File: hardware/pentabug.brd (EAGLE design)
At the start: 82.9 x 33 mm, 19 parts, among them IC1 ATMEGA88

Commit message: bad bug fixed: removed cutout for vibra motor
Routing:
- net GND: track 57.0 -> 25.3 mm
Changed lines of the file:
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@@
 <text x="10.16" y="22.86" size="1.016" layer="25" font="vector" ratio="10">https://github.com/c3d2/pentabug</text>
 <text x="36.195" y="1.27" size="1.016" layer="30" font="vector" ratio="10" rot="MR0">https://github.com/c3d2/pentabug</text>
-<text x="37.465" y="22.86" size="1.4224" layer="30" font="vector" ratio="14" rot="MR0">Pentabug V1.0</text>
+<text x="36.83" y="22.86" size="1.4224" layer="30" font="vector" ratio="14" rot="MR0">Pentabug V1.0</text>
 </plain>
 <attributes>
@@
 <via x="3.81" y="22.86" extent="1-16" drill="0.6" alwaysstop="yes"/>
 <via x="4.445" y="21.59" extent="1-16" drill="0.6" alwaysstop="yes"/>
-<wire x1="4.445" y1="21.59" x2="4.445" y2="11.43" width="1.27" layer="16"/>
 <wire x1="41.91" y1="12.7" x2="41.91" y2="11.43" width="0.6096" layer="1"/>
 <wire x1="41.91" y1="11.43" x2="42.545" y2="10.795" width="0.6096" layer="1"/>
@@
 <wire x1="55.1688" y1="2.1844" x2="52.07" y2="6.35" width="0.6096" layer="1"/>
 <wire x1="52.07" y1="6.35" x2="46.99" y2="7.62" width="0.6096" layer="1"/>
-<wire x1="4.445" y1="21.59" x2="4.445" y2="10.16" width="1.4224" layer="1"/>
 <wire x1="4.445" y1="10.16" x2="3.81" y2="10.16" width="1.4224" layer="1"/>
 <via x="17.145" y="7.62" extent="1-16" drill="0.6"/>
@@
 <via x="48.26" y="3.175" extent="1-16" drill="0.6"/>
 <via x="76.835" y="31.115" extent="1-16" drill="0.6"/>
-<wire x1="8.5" y1="21.59" x2="8.5" y2="11.43" width="1.9304" layer="16"/>
 <via x="5.715" y="8.89" extent="1-16" drill="1.4"/>
 <via x="5.715" y="24.13" extent="1-16" drill="1.4"/>

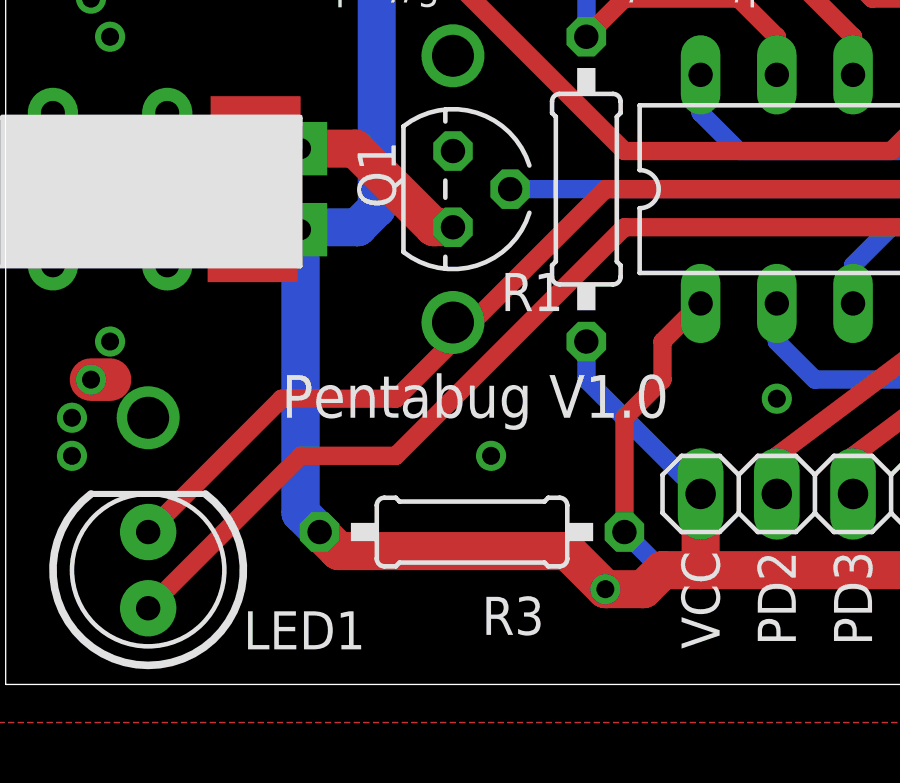
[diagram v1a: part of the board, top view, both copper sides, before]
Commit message: fixed bad bad evil vias connecting Vcc and GND
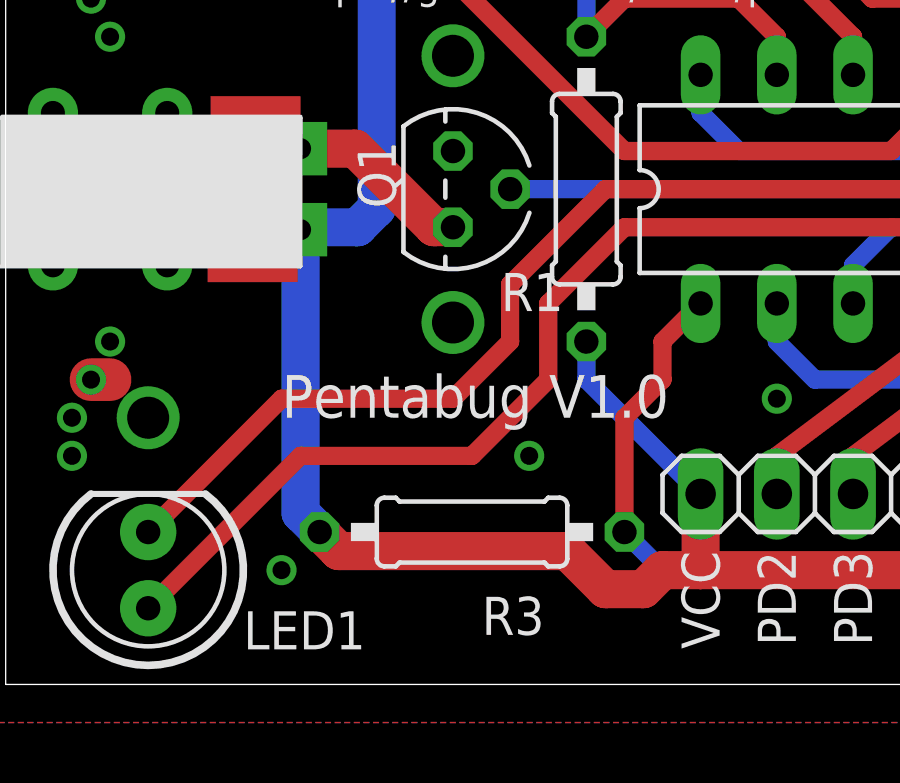
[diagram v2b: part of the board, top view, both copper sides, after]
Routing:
- net N$3: track 39.2 -> 40.7 mm
- net N$10: track 35.6 -> 36.7 mm
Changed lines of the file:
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@@
 <via x="73.66" y="17.78" extent="1-16" drill="0.6"/>
 <via x="73.66" y="20.32" extent="1-16" drill="0.6"/>
-<via x="20.955" y="3.175" extent="1-16" drill="0.6"/>
+<via x="10.16" y="3.81" extent="1-16" drill="0.6"/>
 <via x="3.175" y="7.62" extent="1-16" drill="0.6" alwaysstop="yes"/>
 <via x="3.175" y="8.89" extent="1-16" drill="0.6" alwaysstop="yes"/>
@@
 <wire x1="52.07" y1="6.35" x2="46.99" y2="7.62" width="0.6096" layer="1"/>
 <wire x1="4.445" y1="10.16" x2="3.81" y2="10.16" width="1.4224" layer="1"/>
-<via x="17.145" y="7.62" extent="1-16" drill="0.6"/>
+<via x="18.415" y="7.62" extent="1-16" drill="0.6"/>
 <via x="26.67" y="9.525" extent="1-16" drill="0.6"/>
 <via x="18.415" y="24.765" extent="1-16" drill="0.6"/>
@@
 <wire x1="33.02" y1="15.24" x2="36.83" y2="19.05" width="0.6096" layer="1"/>
 <wire x1="36.83" y1="19.05" x2="36.83" y2="20.32" width="0.6096" layer="1"/>
-<wire x1="21.59" y1="15.24" x2="13.97" y2="7.62" width="0.6096" layer="1"/>
-<wire x1="13.97" y1="7.62" x2="10.795" y2="7.62" width="0.6096" layer="1"/>
+<wire x1="16.51" y1="7.62" x2="10.795" y2="7.62" width="0.6096" layer="1"/>
+<wire x1="21.59" y1="15.24" x2="19.05" y2="12.7" width="0.6096" layer="1"/>
+<wire x1="19.05" y1="12.7" x2="19.05" y2="10.16" width="0.6096" layer="1"/>
+<wire x1="19.05" y1="10.16" x2="16.51" y2="7.62" width="0.6096" layer="1"/>
 </signal>
 <signal name="N$5">
@@
 <wire x1="31.75" y1="16.51" x2="34.29" y2="19.05" width="0.6096" layer="1"/>
 <wire x1="34.29" y1="19.05" x2="34.29" y2="20.32" width="0.6096" layer="1"/>
-<wire x1="20.955" y1="16.51" x2="13.97" y2="9.525" width="0.6096" layer="1"/>
-<wire x1="13.97" y1="9.525" x2="10.16" y2="9.525" width="0.6096" layer="1"/>
+<wire x1="15.875" y1="9.525" x2="10.16" y2="9.525" width="0.6096" layer="1"/>
+<wire x1="20.955" y1="16.51" x2="17.78" y2="13.335" width="0.6096" layer="1"/>
+<wire x1="17.78" y1="13.335" x2="17.78" y2="11.43" width="0.6096" layer="1"/>
+<wire x1="17.78" y1="11.43" x2="15.875" y2="9.525" width="0.6096" layer="1"/>
 </signal>
 <signal name="BATTLVL">

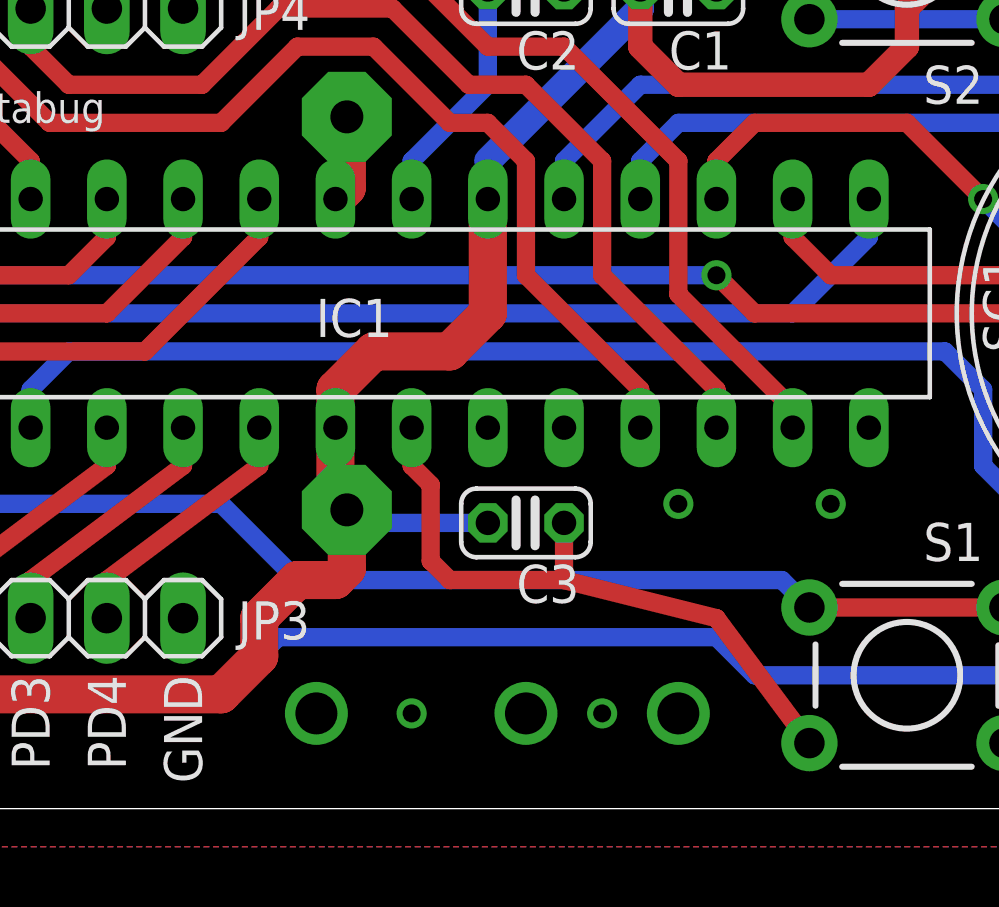
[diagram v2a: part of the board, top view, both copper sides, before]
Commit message: c3 closer to uC, "resistor" between avcc and vcc
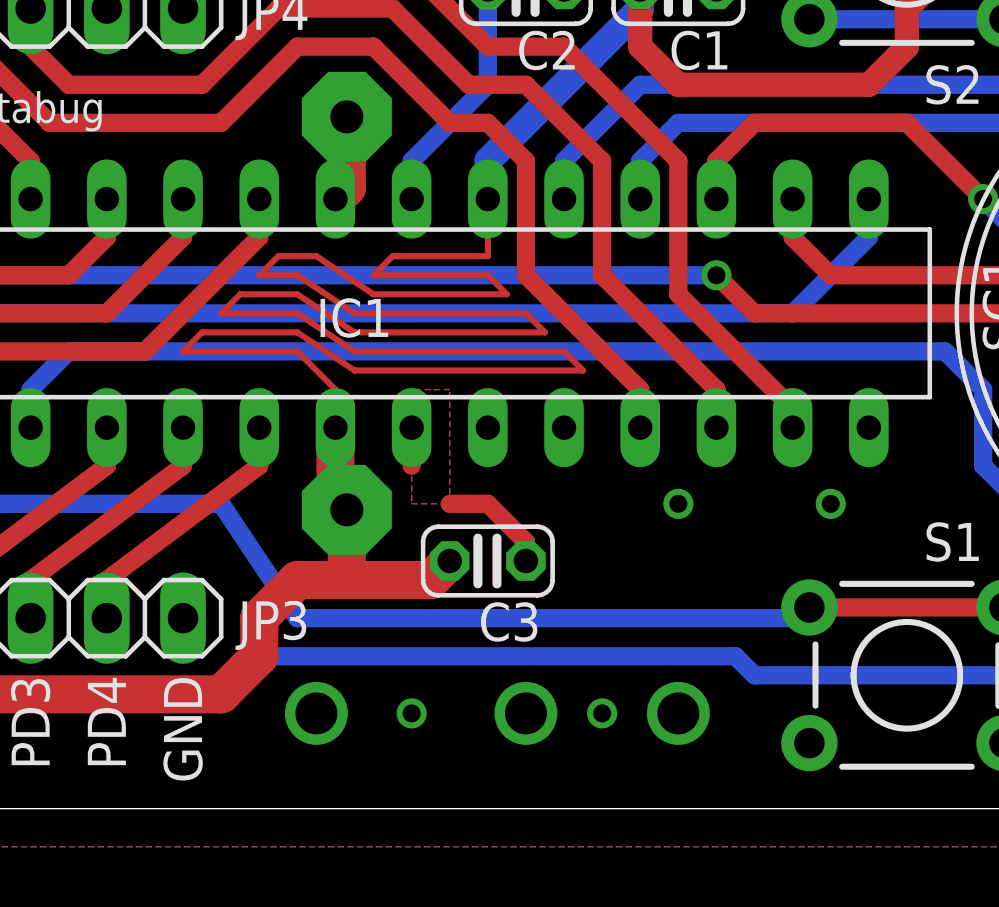
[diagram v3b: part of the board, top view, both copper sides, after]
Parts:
- moved C3 1.80 mm to (44.5, 8.26)
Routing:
- net VCC: track 142.5 -> 205.3 mm
- net GND: track 25.3 -> 8.50 mm, vias 42 -> 44
- net RX: track 51.0 -> 51.8 mm
- net RST: track 81.2 -> 80.7 mm
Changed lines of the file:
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@@
 <layer number="21" name="tPlace" color="7" fill="1" visible="yes" active="yes"/>
 <layer number="22" name="bPlace" color="7" fill="1" visible="yes" active="yes"/>
-<layer number="23" name="tOrigins" color="15" fill="1" visible="no" active="yes"/>
-<layer number="24" name="bOrigins" color="15" fill="1" visible="no" active="yes"/>
-<layer number="25" name="tNames" color="7" fill="1" visible="yes" active="yes"/>
-<layer number="26" name="bNames" color="7" fill="1" visible="no" active="yes"/>
+<layer number="23" name="tOrigins" color="15" fill="1" visible="yes" active="yes"/>
+<layer number="24" name="bOrigins" color="15" fill="1" visible="yes" active="yes"/>
+<layer number="25" name="tNames" color="7" fill="1" visible="no" active="yes"/>
+<layer number="26" name="bNames" color="7" fill="1" visible="yes" active="yes"/>
 <layer number="27" name="tValues" color="7" fill="1" visible="no" active="yes"/>
 <layer number="28" name="bValues" color="7" fill="1" visible="no" active="yes"/>
@@
 <param name="mdDrill" value="8mil"/>
 <param name="mdSmdStop" value="0mil"/>
-<param name="msWidth" value="10mil"/>
+<param name="msWidth" value="8mil"/>
 <param name="msDrill" value="0.6mm"/>
 <param name="msMicroVia" value="9.99mm"/>
@@
 <attribute name="NAME" x="60.96" y="9.525" size="1.27" layer="25" font="vector" ratio="10" rot="R180"/>
 </element>
-<element name="C3" library="resistor" package="C025-024X044" value="100nF" x="45.72" y="9.525" smashed="yes" rot="R180">
-<attribute name="NAME" x="47.498" y="8.128" size="1.27" layer="25" font="vector" ratio="10" rot="R180"/>
-<attribute name="VALUE" x="47.498" y="12.192" size="1.27" layer="27" ratio="10" rot="R180"/>
+<element name="C3" library="resistor" package="C025-024X044" value="100nF" x="44.45" y="8.255" smashed="yes" rot="R180">
+<attribute name="NAME" x="46.228" y="6.858" size="1.27" layer="25" font="vector" ratio="10" rot="R180"/>
+<attribute name="VALUE" x="46.228" y="10.922" size="1.27" layer="27" ratio="10" rot="R180"/>
 </element>
 <element name="Q1" library="transistors" package="TO-92" value="" x="15.875" y="16.51" smashed="yes" rot="R270">
@@
 </element>
 <element name="BAT1" library="seb" package="BATTERY_2XAAA" value="BATTERY_2XAAA" x="63.5" y="16.51" smashed="yes" rot="MR180">
-<attribute name="NAME" x="36.83" y="3.048" size="1.27" layer="26" font="vector" ratio="10" rot="MR180"/>
+<attribute name="NAME" x="60.325" y="2.667" size="1.27" layer="26" font="vector" ratio="10" rot="MR0"/>
 <attribute name="VALUE" x="36.83" y="32.385" size="1.778" layer="28" font="vector" ratio="10" rot="MR180"/>
 </element>
@@
 <contactref element="BAT1" pad="+"/>
 <contactref element="U$1" pad="P$1"/>
-<wire x1="39.37" y1="12.7" x2="39.37" y2="13.97" width="1.27" layer="1"/>
-<wire x1="39.37" y1="13.97" x2="40.64" y2="15.24" width="1.27" layer="1"/>
-<wire x1="40.64" y1="15.24" x2="43.18" y2="15.24" width="1.27" layer="1"/>
-<wire x1="43.18" y1="15.24" x2="44.45" y2="16.51" width="1.27" layer="1"/>
-<wire x1="44.45" y1="16.51" x2="44.45" y2="20.32" width="1.27" layer="1"/>
 <wire x1="44.45" y1="20.32" x2="44.45" y2="21.59" width="0.6096" layer="16"/>
 <wire x1="44.45" y1="21.59" x2="49.53" y2="26.67" width="0.9144" layer="16"/>
@@
 <wire x1="62.865" y1="28.575" x2="63.805" y2="27.635" width="0.8128" layer="1"/>
 <wire x1="67.945" y1="27.635" x2="70.79" y2="30.48" width="0.8128" layer="1"/>
-<wire x1="44.45" y1="9.525" x2="40.185" y2="9.525" width="0.6096" layer="16"/>
-<wire x1="40.185" y1="9.525" x2="39.75" y2="9.96" width="0.6096" layer="16"/>
+<wire x1="43.18" y1="8.255" x2="42.545" y2="7.62" width="1.27" layer="1"/>
+<wire x1="42.545" y1="7.62" x2="39.37" y2="7.62" width="1.27" layer="1"/>
+<wire x1="39.37" y1="12.7" x2="39.37" y2="13.97" width="0.2032" layer="1"/>
+<wire x1="39.37" y1="13.97" x2="38.1" y2="15.24" width="0.2032" layer="1"/>
+<wire x1="38.1" y1="15.24" x2="34.29" y2="15.24" width="0.2032" layer="1"/>
+<wire x1="34.29" y1="15.24" x2="34.925" y2="15.875" width="0.2032" layer="1"/>
+<wire x1="34.925" y1="15.875" x2="38.1" y2="15.875" width="0.2032" layer="1"/>
+<wire x1="38.1" y1="15.875" x2="40.005" y2="14.605" width="0.2032" layer="1"/>
+<wire x1="40.005" y1="14.605" x2="47.625" y2="14.605" width="0.2032" layer="1"/>
+<wire x1="47.625" y1="14.605" x2="46.99" y2="15.24" width="0.2032" layer="1"/>
+<wire x1="46.99" y1="15.24" x2="40.005" y2="15.24" width="0.2032" layer="1"/>
+<wire x1="40.005" y1="15.24" x2="38.1" y2="16.51" width="0.2032" layer="1"/>
+<wire x1="38.1" y1="16.51" x2="35.56" y2="16.51" width="0.2032" layer="1"/>
+<wire x1="35.56" y1="16.51" x2="36.195" y2="17.145" width="0.2032" layer="1"/>
+<wire x1="36.195" y1="17.145" x2="38.1" y2="17.145" width="0.2032" layer="1"/>
+<wire x1="38.1" y1="17.145" x2="40.005" y2="15.875" width="0.2032" layer="1"/>
+<wire x1="40.005" y1="15.875" x2="46.355" y2="15.875" width="0.2032" layer="1"/>
+<wire x1="46.355" y1="15.875" x2="45.72" y2="16.51" width="0.2032" layer="1"/>
+<wire x1="45.72" y1="16.51" x2="40.005" y2="16.51" width="0.2032" layer="1"/>
+<wire x1="40.005" y1="16.51" x2="38.1" y2="17.78" width="0.2032" layer="1"/>
+<wire x1="38.1" y1="17.78" x2="36.83" y2="17.78" width="0.2032" layer="1"/>
+<wire x1="36.83" y1="17.78" x2="37.465" y2="18.415" width="0.2032" layer="1"/>
+<wire x1="37.465" y1="18.415" x2="38.735" y2="18.415" width="0.2032" layer="1"/>
+<wire x1="38.735" y1="18.415" x2="40.64" y2="17.145" width="0.2032" layer="1"/>
+<wire x1="40.64" y1="17.145" x2="45.085" y2="17.145" width="0.2032" layer="1"/>
+<wire x1="45.085" y1="17.145" x2="44.45" y2="17.78" width="0.2032" layer="1"/>
+<wire x1="44.45" y1="17.78" x2="40.64" y2="17.78" width="0.2032" layer="1"/>
+<wire x1="40.64" y1="17.78" x2="41.275" y2="18.415" width="0.2032" layer="1"/>
+<wire x1="41.275" y1="18.415" x2="44.45" y2="18.415" width="0.2032" layer="1"/>
+<wire x1="44.45" y1="18.415" x2="44.45" y2="20.32" width="0.2032" layer="1"/>
 </signal>
 <signal name="GND">
@@
 <via x="3.81" y="22.86" extent="1-16" drill="0.6" alwaysstop="yes"/>
 <via x="4.445" y="21.59" extent="1-16" drill="0.6" alwaysstop="yes"/>
-<wire x1="41.91" y1="12.7" x2="41.91" y2="11.43" width="0.6096" layer="1"/>
-<wire x1="41.91" y1="11.43" x2="42.545" y2="10.795" width="0.6096" layer="1"/>
-<wire x1="42.545" y1="10.795" x2="42.545" y2="8.255" width="0.6096" layer="1"/>
-<wire x1="42.545" y1="8.255" x2="43.18" y2="7.62" width="0.6096" layer="1"/>
-<wire x1="43.18" y1="7.62" x2="46.99" y2="7.62" width="0.6096" layer="1"/>
-<wire x1="46.99" y1="7.62" x2="46.99" y2="9.525" width="0.6096" layer="1"/>
-<wire x1="55.1688" y1="2.1844" x2="52.07" y2="6.35" width="0.6096" layer="1"/>
-<wire x1="52.07" y1="6.35" x2="46.99" y2="7.62" width="0.6096" layer="1"/>
 <wire x1="4.445" y1="10.16" x2="3.81" y2="10.16" width="1.4224" layer="1"/>
 <via x="18.415" y="7.62" extent="1-16" drill="0.6"/>
@@
 <via x="15.875" y="20.955" extent="1-16" drill="1.4"/>
 <via x="15.875" y="12.065" extent="1-16" drill="1.4"/>
+<wire x1="41.91" y1="12.7" x2="41.91" y2="11.43" width="0.6096" layer="1"/>
+<wire x1="43.18" y1="10.16" x2="44.45" y2="10.16" width="0.6096" layer="1"/>
+<wire x1="44.45" y1="10.16" x2="45.72" y2="8.89" width="0.6096" layer="1"/>
+<wire x1="45.72" y1="8.89" x2="45.72" y2="8.255" width="0.6096" layer="1"/>
+<via x="50.8" y="10.16" extent="1-16" drill="0.6"/>
+<via x="55.88" y="10.16" extent="1-16" drill="0.6"/>
+<polygon width="0.2032" layer="16" thermals="no">
+<vertex x="41.91" y="13.97"/>
+<vertex x="41.91" y="10.16"/>
+<vertex x="43.18" y="10.16"/>
+<vertex x="43.18" y="13.97"/>
+</polygon>
+<polygon width="0.2032" layer="1" thermals="no">
+<vertex x="41.91" y="13.97"/>
+<vertex x="41.91" y="10.16"/>
+<vertex x="43.18" y="10.16"/>
+<vertex x="43.18" y="13.97"/>
+</polygon>
 </signal>
 <signal name="N$17">
@@
 <wire x1="27.94" y1="10.16" x2="26.67" y2="11.43" width="0.6096" layer="16"/>
 <wire x1="26.67" y1="11.43" x2="26.67" y2="12.7" width="0.6096" layer="16"/>
-<wire x1="38.1" y1="7.62" x2="54.2544" y2="7.62" width="0.6096" layer="16"/>
-<wire x1="54.2544" y1="7.62" x2="55.1688" y2="6.7056" width="0.6096" layer="16"/>
-<wire x1="35.56" y1="10.16" x2="38.1" y2="7.62" width="0.6096" layer="16"/>
+<wire x1="38.1" y1="6.35" x2="54.8132" y2="6.35" width="0.6096" layer="16"/>
 <wire x1="61.6712" y1="6.7056" x2="70.76929375" y2="6.7056" width="0.6096" layer="1"/>
 <wire x1="70.76929375" y1="6.7056" x2="73.393946875" y2="4.080946875" width="0.6096" layer="1"/>
+<wire x1="38.1" y1="6.35" x2="35.56" y2="10.16" width="0.6096" layer="16"/>
+<wire x1="54.8132" y1="6.35" x2="55.1688" y2="6.7056" width="0.6096" layer="16"/>
 </signal>
 <signal name="N$3">
@@
 <wire x1="21.59" y1="5.08" x2="22.86" y2="3.81" width="0.6096" layer="16"/>
 <wire x1="22.86" y1="3.81" x2="35.56" y2="3.81" width="0.6096" layer="16"/>
-<wire x1="37.465" y1="5.715" x2="35.56" y2="3.81" width="0.6096" layer="16"/>
 <wire x1="64.135" y1="4.445" x2="53.34" y2="4.445" width="0.6096" layer="16"/>
-<wire x1="53.34" y1="4.445" x2="52.07" y2="5.715" width="0.6096" layer="16"/>
-<wire x1="52.07" y1="5.715" x2="37.465" y2="5.715" width="0.6096" layer="16"/>
+<wire x1="52.705" y1="5.08" x2="36.83" y2="5.08" width="0.6096" layer="16"/>
 <wire x1="64.135" y1="4.445" x2="66.04" y2="6.35" width="0.6096" layer="16"/>
 <wire x1="66.04" y1="6.35" x2="69.85" y2="6.35" width="0.6096" layer="16"/>
@@
 <wire x1="22.86" y1="10.16" x2="21.59" y2="8.89" width="0.6096" layer="1"/>
 <wire x1="21.59" y1="8.89" x2="21.59" y2="5.08" width="0.6096" layer="1"/>
+<wire x1="52.705" y1="5.08" x2="53.34" y2="4.445" width="0.6096" layer="16"/>
+<wire x1="36.83" y1="5.08" x2="35.56" y2="3.81" width="0.6096" layer="16"/>
 </signal>
 <signal name="MOSI">
@@
 <wire x1="31.75" y1="27.94" x2="31.75" y2="26.67" width="0.6096" layer="1"/>
 </signal>
-<signal name="N$13">
-<via x="50.8" y="10.16" extent="1-16" drill="0.6"/>
-</signal>
-<signal name="N$14">
-<via x="55.88" y="10.16" extent="1-16" drill="0.6"/>
-</signal>
 <signal name="N$1">
